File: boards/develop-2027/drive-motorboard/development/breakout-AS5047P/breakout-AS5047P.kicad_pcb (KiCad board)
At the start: 2 copper layers, 0 parts

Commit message: add AS5047 breakout board
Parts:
- added C1: 100n, Capacitor_SMD:C_0603_1608Metric_Pad1.08x0.95mm_HandSolder, F.Cu at (115.5, 50.0)
- added G***: LOGO, RJ-Graphics:GRAPHIC_PIMAN_LINK_LOGO_CU, F.Cu at (110.0, 61.5)
- added H1: Motor Mount, MountingHole:MountingHole_3.2mm_M3_Pad, F.Cu at (90.0, 30.0)
- added H2: Motor Mount, MountingHole:MountingHole_3.2mm_M3_Pad, F.Cu at (130.0, 30.0)
- added H3: Motor Mount, MountingHole:MountingHole_3.2mm_M3_Pad, F.Cu at (130.0, 70.0)
- added H4: Motor Mount, MountingHole:MountingHole_3.2mm_M3_Pad, F.Cu at (90.0, 70.0)
- added J1: Left Header, Connector_PinHeader_2.54mm:PinHeader_1x06_P2.54mm_Vertical, B.Cu at (99.8, 43.6)
- added J2: Right Header, Connector_PinHeader_2.54mm:PinHeader_1x06_P2.54mm_Vertical, B.Cu at (120.2, 43.6)
- added U1: AS5047P, Package_SO:TSSOP-14_4.4x5mm_P0.65mm, F.Cu at (110.0, 50.0)
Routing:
- net +3.3V: track 0.00 -> 11.0 mm
- net GND: track 0.00 -> 10.1 mm
- net /~{SPI_CS}: track 0.00 -> 9.12 mm
- net /PWM: track 0.00 -> 9.12 mm
- net /ENC_I: track 0.00 -> 9.12 mm
- net /ENC_A: track 0.00 -> 9.12 mm
- net /SPI_CLK: track 0.00 -> 8.34 mm
- net /ENC_B: track 0.00 -> 8.34 mm
- net /SPI_MOSI: track 0.00 -> 7.82 mm
- net /SPI_MISO: track 0.00 -> 7.55 mm
- added copper zone on F.Cu, net GND
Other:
- board outline added: 50 x 50 mm
- board text added: "40 mm"
- board text added: "AS5047P Dev Board"
- board text added: "CS CLK MOSI MIS0 ENCA ENCB"
- board text added: "ENCI 3.3V 3.3V GND GND PWM"

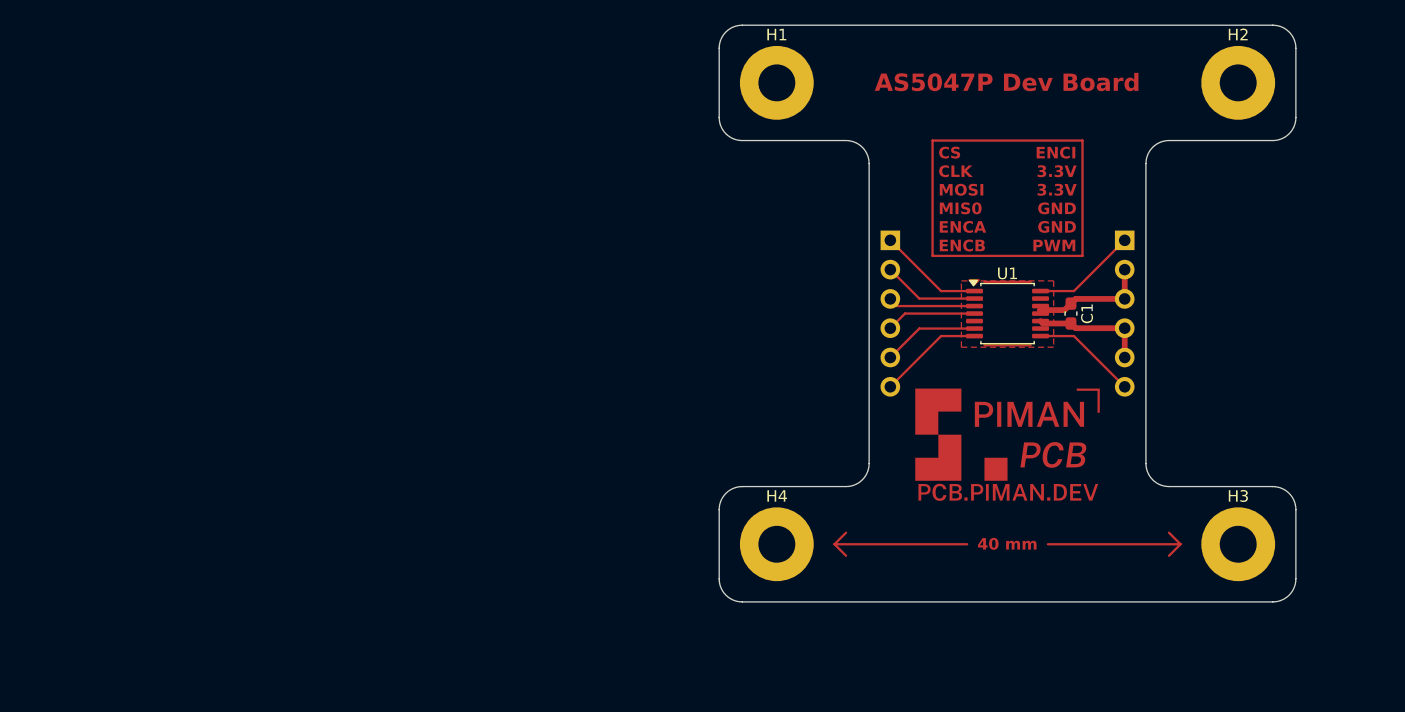
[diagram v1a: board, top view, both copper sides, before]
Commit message: v1.1 - leave unused U/V floating instead of drive low
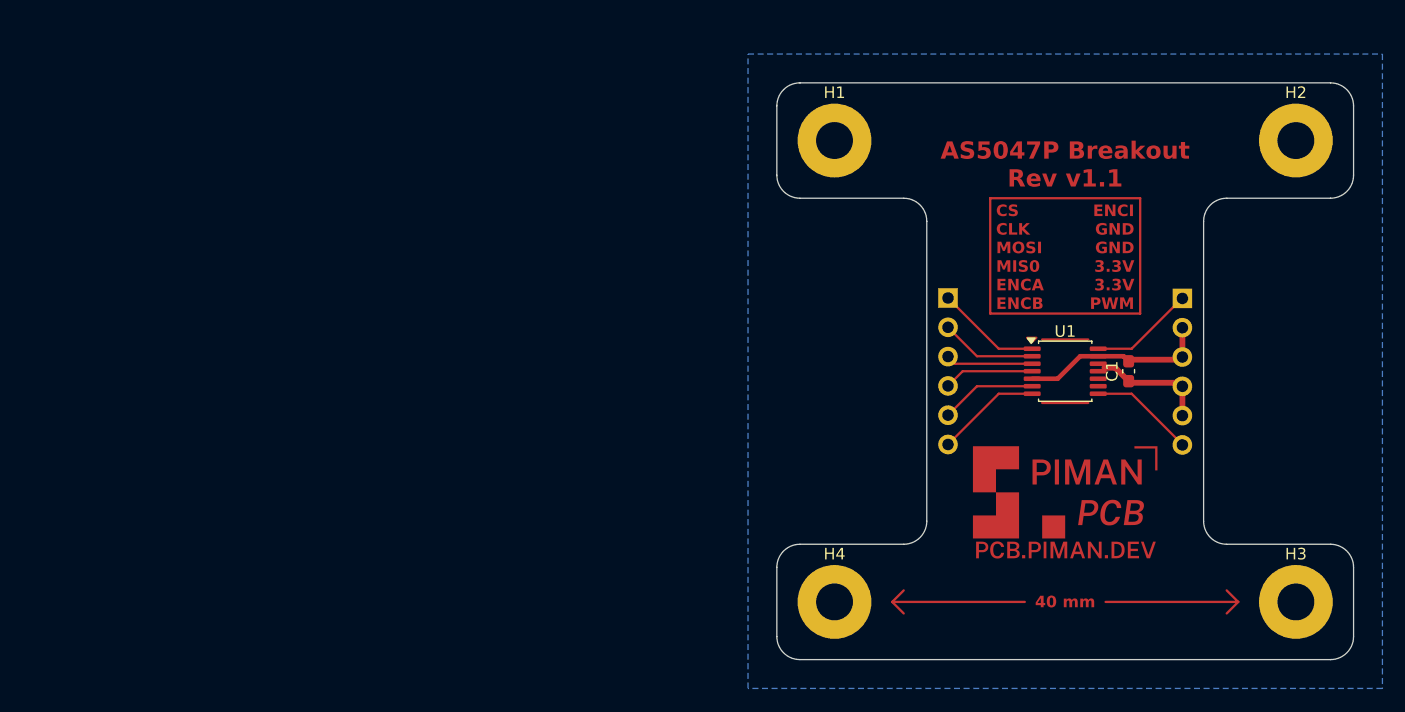
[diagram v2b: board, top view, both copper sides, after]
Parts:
- moved J2 7.10 mm to (125.2, 48.7)
- moved C1 7.07 mm to (120.5, 55.0), turned to 90 degrees
- moved G*** 7.07 mm to (115.0, 66.5)
- moved H1 7.07 mm to (95.0, 35.0)
- moved H2 7.07 mm to (135.0, 35.0)
- moved H3 7.07 mm to (135.0, 75.0)
- moved H4 7.07 mm to (95.0, 75.0)
- moved J1 7.07 mm to (104.8, 48.6)
- moved U1 7.07 mm to (115.0, 55.0)
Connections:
- J2 pad 2: +3.3V -> GND
- J2 pad 3: +3.3V -> GND
- J2 pad 4: GND -> +3.3V
- J2 pad 5: GND -> +3.3V
- U1 pad 10: GND -> unconnected-(U1-U-Pad10)
- U1 pad 9: GND -> unconnected-(U1-V-Pad9)
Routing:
- net GND: track 10.1 -> 16.7 mm
- net +3.3V: track 11.0 -> 9.97 mm
- added copper zone on B.Cu, net (none)
- removed copper zone on F.Cu, net GND
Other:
- board text added: "AS5047P Breakout Rev v1.1"
- board text added: "ENCI GND GND 3.3V 3.3V PWM"
- board text removed: "AS5047P Dev Board"
- board text removed: "ENCI 3.3V 3.3V GND GND PWM"

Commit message: add manufacturing notes for 1.1
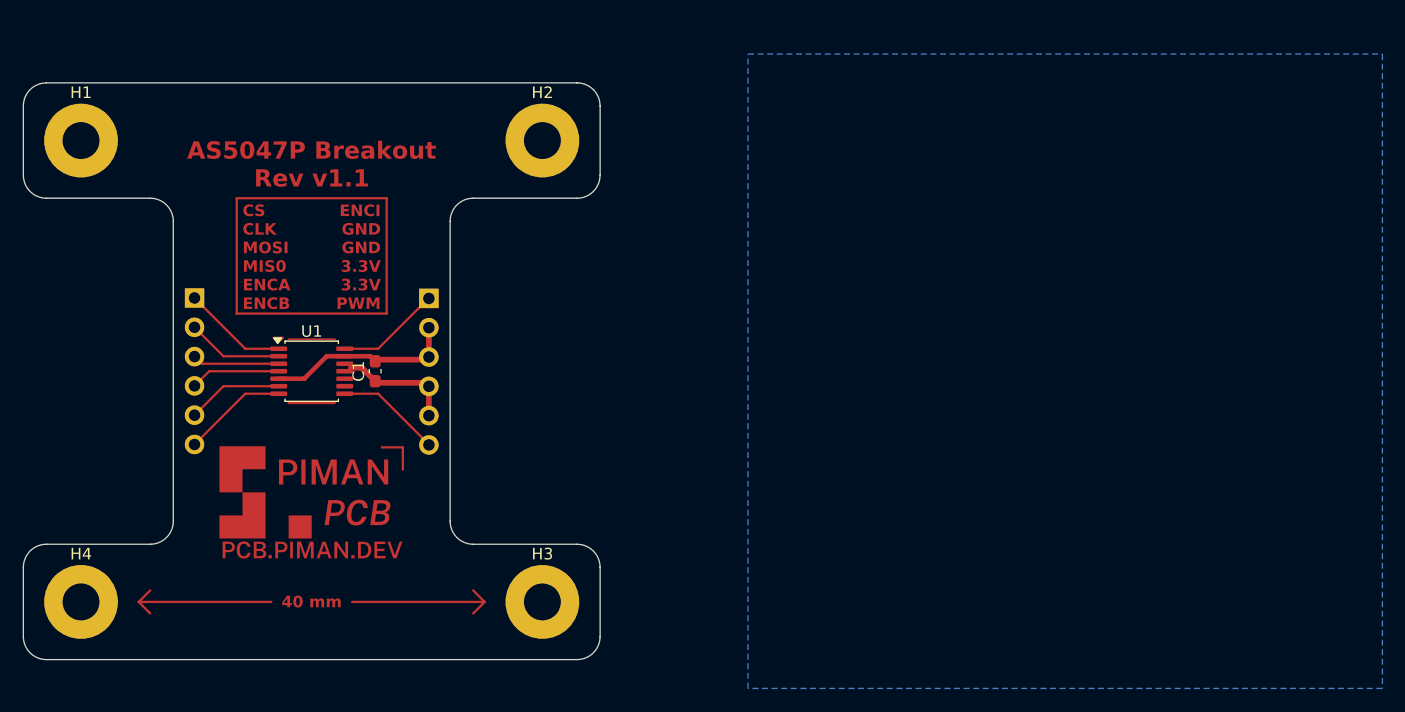
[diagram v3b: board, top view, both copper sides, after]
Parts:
- moved C1 65.3 mm to (55.2, 55.0)
- moved G*** 65.3 mm to (49.7, 66.5)
- moved H1 65.3 mm to (29.7, 35.0)
- moved H2 65.3 mm to (69.7, 35.0)
- moved H3 65.3 mm to (69.7, 75.0)
- moved H4 65.3 mm to (29.7, 75.0)
- moved J1 65.3 mm to (39.5, 48.6)
- moved U1 65.3 mm to (49.7, 55.0)
- moved J2 65.3 mm to (59.8, 48.7)

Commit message: fix pcb formatting
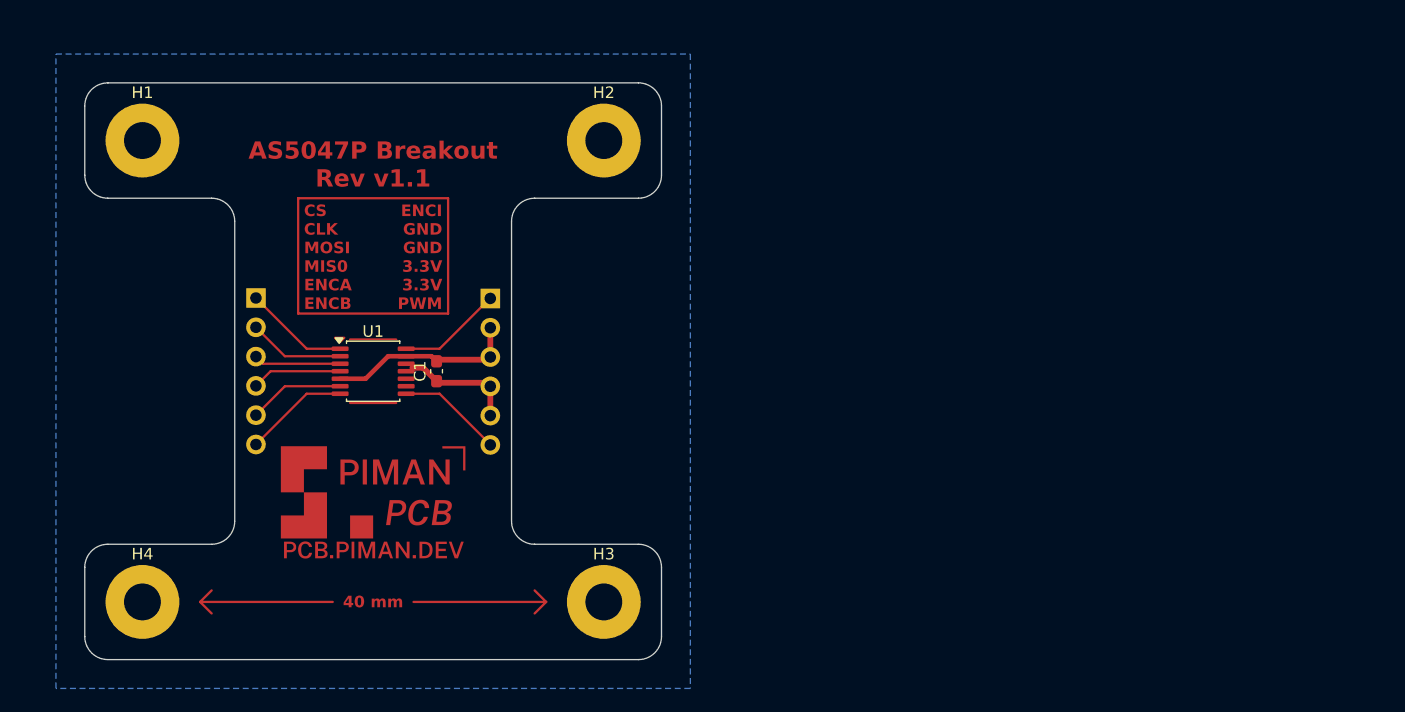
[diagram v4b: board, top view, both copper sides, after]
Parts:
- moved C1 5.33 mm to (60.5, 55.0)
- moved G*** 5.33 mm to (55.0, 66.5)
- moved H2 5.33 mm to (75.0, 35.0)
- moved H3 5.33 mm to (75.0, 75.0)
- moved J1 5.33 mm to (44.8, 48.6)
- moved U1 5.33 mm to (55.0, 55.0)
- moved H1 5.32 mm to (35.0, 35.0)
- moved H4 5.32 mm to (35.0, 75.0)
- moved J2 5.32 mm to (65.2, 48.7)
